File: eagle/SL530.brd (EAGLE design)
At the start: 100 x 100 mm, 42 parts, among them IC4 74LVC1G17DBV, IC5 74LVC1G17DBV, U1 LM1117, X1 MC68000

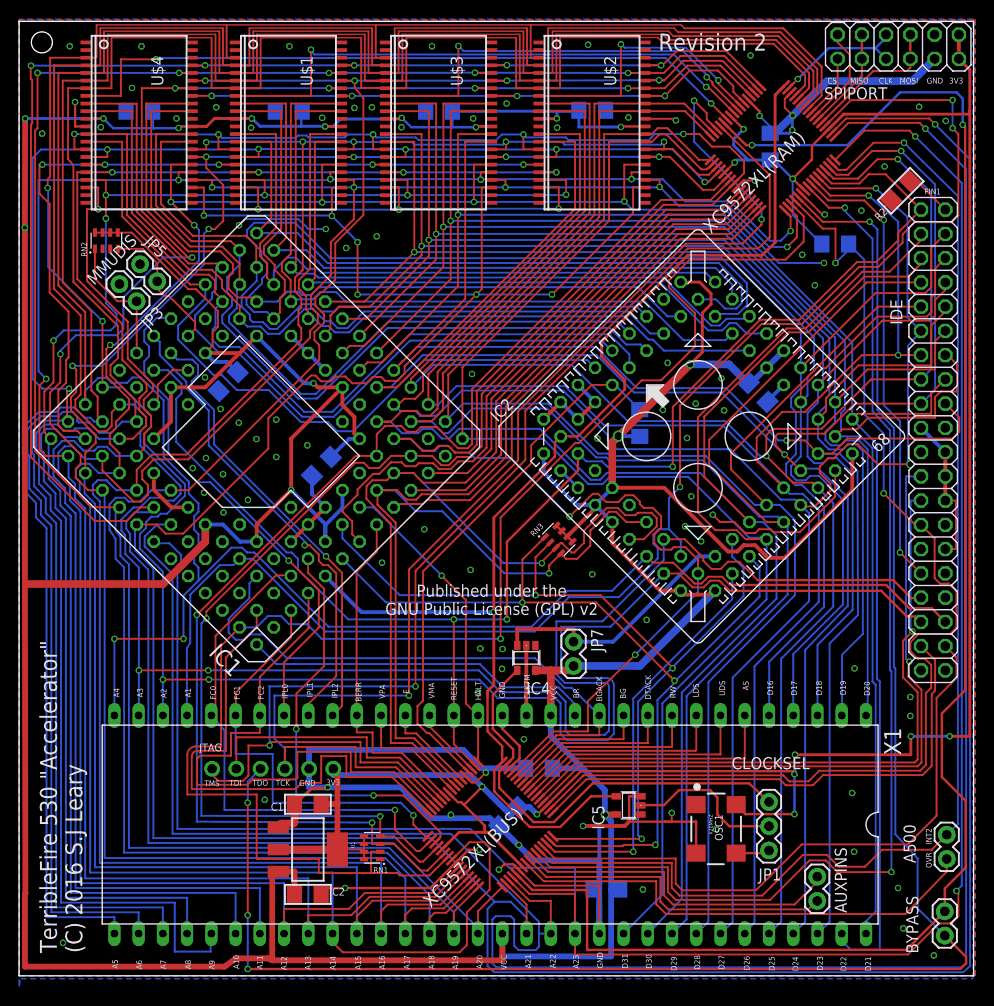
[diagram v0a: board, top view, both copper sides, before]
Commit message: Updated silkscreen
Added the CPLD orientation marks
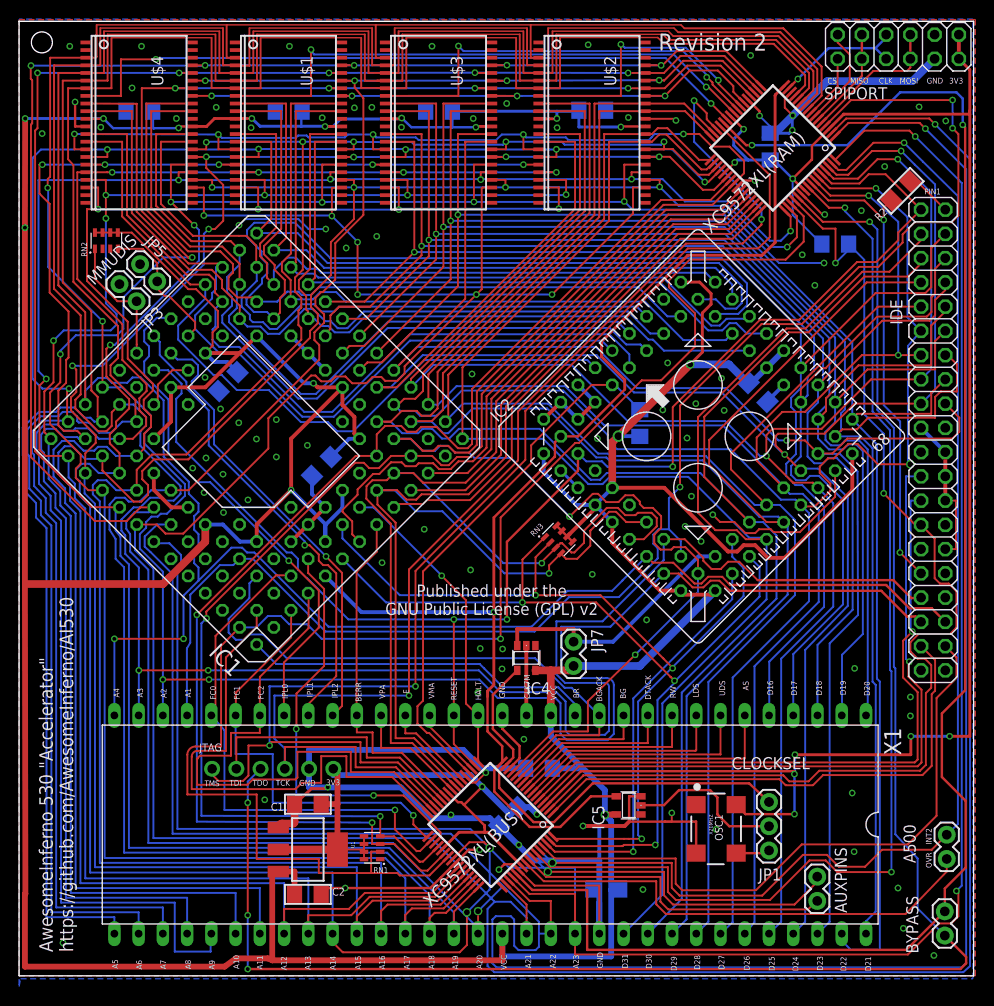
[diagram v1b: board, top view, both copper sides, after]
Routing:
- net INT2: vias 1 -> 2
- net AUX0: vias 0 -> 1
- net A20: vias 5 -> 6
- net A14: vias 7 -> 9
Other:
- board text added: "AwesomeInferno 530 "Accelerator" https://github.com/AwesomeInferno/AI530"
- board text removed: "TerribleFire 530 "Accelerator" (C) 2016 S.J Leary"
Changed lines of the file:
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@@
 <?xml version="1.0" encoding="utf-8"?>
 <!DOCTYPE eagle SYSTEM "eagle.dtd">
-<eagle version="7.7.0">
+<eagle version="7.6.0">
 <drawing>
 <settings>
@@
 <layer number="17" name="Pads" color="2" fill="1" visible="yes" active="yes"/>
 <layer number="18" name="Vias" color="2" fill="1" visible="yes" active="yes"/>
-<layer number="19" name="Unrouted" color="6" fill="1" visible="yes" active="yes"/>
+<layer number="19" name="Unrouted" color="6" fill="1" visible="no" active="yes"/>
 <layer number="20" name="Dimension" color="15" fill="1" visible="yes" active="yes"/>
 <layer number="21" name="tPlace" color="7" fill="1" visible="yes" active="yes"/>
-<layer number="22" name="bPlace" color="7" fill="1" visible="yes" active="yes"/>
-<layer number="23" name="tOrigins" color="15" fill="1" visible="yes" active="yes"/>
-<layer number="24" name="bOrigins" color="15" fill="1" visible="yes" active="yes"/>
+<layer number="22" name="bPlace" color="7" fill="1" visible="no" active="yes"/>
+<layer number="23" name="tOrigins" color="15" fill="1" visible="no" active="yes"/>
+<layer number="24" name="bOrigins" color="15" fill="1" visible="no" active="yes"/>
 <layer number="25" name="tNames" color="7" fill="1" visible="yes" active="yes"/>
 <layer number="26" name="bNames" color="7" fill="1" visible="yes" active="yes"/>
-<layer number="27" name="tValues" color="7" fill="1" visible="yes" active="yes"/>
-<layer number="28" name="bValues" color="7" fill="1" visible="yes" active="yes"/>
+<layer number="27" name="tValues" color="7" fill="1" visible="no" active="yes"/>
+<layer number="28" name="bValues" color="7" fill="1" visible="no" active="yes"/>
 <layer number="29" name="tStop" color="7" fill="3" visible="no" active="yes"/>
 <layer number="30" name="bStop" color="7" fill="6" visible="no" active="yes"/>
@@
 <layer number="49" name="Reference" color="7" fill="1" visible="no" active="yes"/>
 <layer number="50" name="dxf" color="7" fill="1" visible="no" active="no"/>
-<layer number="51" name="tDocu" color="7" fill="1" visible="yes" active="yes"/>
-<layer number="52" name="bDocu" color="7" fill="1" visible="yes" active="yes"/>
+<layer number="51" name="tDocu" color="7" fill="1" visible="no" active="yes"/>
+<layer number="52" name="bDocu" color="7" fill="1" visible="no" active="yes"/>
 <layer number="53" name="tGND_GNDA" color="7" fill="9" visible="no" active="no"/>
 <layer number="54" name="bGND_GNDA" color="1" fill="9" visible="no" active="no"/>
@@
 <text x="21.0058" y="20.4724" size="0.6096" layer="25" rot="R180">TMS</text>
 <text x="28.3718" y="20.5232" size="0.6096" layer="25" rot="R180">TCK</text>
-<text x="6.6294" y="2.3876" size="1.778" layer="25" rot="R90">TerribleFire 530 "Accelerator"
-(C) 2016 S.J Leary</text>
+<text x="5.6642" y="2.4892" size="1.4224" layer="25" rot="R90">AwesomeInferno 530 "Accelerator"
+https://github.com/AwesomeInferno/AI530</text>
 <text x="66.9798" y="96.9264" size="1.778" layer="25">Revision 2</text>
 <text x="73.406" y="75.2094" size="0.8128" layer="125" ratio="18" rot="R180">C1</text>
@@
 <text x="98.9076" y="94.0816" size="0.6096" layer="25" rot="R180">3V3</text>
 <text x="96.5454" y="82.4738" size="0.6096" layer="25" rot="R180">PIN1</text>
+<wire x1="72.4662" y1="86.7664" x2="78.9686" y2="93.2688" width="0.254" layer="21"/>
+<wire x1="78.9686" y1="93.2688" x2="85.471" y2="86.7664" width="0.254" layer="21"/>
+<wire x1="85.471" y1="86.7664" x2="85.471" y2="86.6902" width="0.127" layer="21"/>
+<wire x1="85.471" y1="86.6902" x2="78.9686" y2="80.1878" width="0.254" layer="21"/>
+<wire x1="78.9686" y1="80.1878" x2="72.4154" y2="86.741" width="0.254" layer="21"/>
+<circle x="84.455" y="86.741" radius="0.297296875" width="0.127" layer="21"/>
+<circle x="54.864" y="15.8496" radius="0.297296875" width="0.127" layer="21"/>
+<wire x1="42.8498" y1="15.9004" x2="42.9006" y2="15.9004" width="0.127" layer="21"/>
+<wire x1="42.9006" y1="15.9004" x2="49.3522" y2="22.3012" width="0.254" layer="21"/>
+<wire x1="49.3522" y1="22.3012" x2="55.9308" y2="15.7226" width="0.254" layer="21"/>
+<wire x1="55.9308" y1="15.7226" x2="55.88" y2="15.7226" width="0.127" layer="21"/>
+<wire x1="55.88" y1="15.7226" x2="49.4792" y2="9.3218" width="0.254" layer="21"/>
+<wire x1="49.4792" y1="9.3218" x2="49.4284" y2="9.3218" width="0.127" layer="21"/>
+<wire x1="49.4284" y1="9.3218" x2="42.9006" y2="15.8496" width="0.254" layer="21"/>
 </plain>
 <attributes>
@@
 <wire x1="68.8848" y1="96.8756" x2="74.0865" y2="96.8756" width="0.2032" layer="1"/>
 <wire x1="74.0865" y1="96.8756" x2="77.7057625" y2="93.2563375" width="0.2032" layer="1"/>
-<wire x1="50.615034375" y1="9.308859375" x2="48.0822" y2="6.776025" width="0.2032" layer="1"/>
+<wire x1="50.615034375" y1="9.308859375" x2="48.0822" y2="6.776025" width="0.2032" layer="16"/>
 <wire x1="1.2446" y1="54.3306" x2="1.2446" y2="89.1794" width="0.2032" layer="1"/>
 <wire x1="1.2446" y1="89.1794" x2="1.3716" y2="89.3064" width="0.2032" layer="1"/>
@@
 <wire x1="1.2192" y1="95.3262" x2="1.2446" y2="95.3516" width="0.2032" layer="1"/>
 <wire x1="1.2446" y1="54.3306" x2="7.9248" y2="47.6504" width="0.2032" layer="1"/>
+<via x="48.0822" y="6.776025" extent="1-16" drill="0.6" shape="square"/>
 </signal>
 <signal name="A19">
@@
 <wire x1="47.169846875" y1="13.9954" x2="48.7172" y2="13.9954" width="0.2032" layer="1"/>
 <wire x1="48.7172" y1="13.9954" x2="49.3014" y2="13.4112" width="0.2032" layer="1"/>
-<wire x1="49.3014" y1="13.4112" x2="49.3014" y2="9.0424" width="0.2032" layer="1"/>
-<wire x1="49.3014" y1="9.0424" x2="46.9138" y2="6.6548" width="0.2032" layer="1"/>
+<wire x1="49.3014" y1="13.4112" x2="49.3014" y2="9.0424" width="0.2032" layer="16"/>
+<wire x1="49.3014" y1="9.0424" x2="46.9138" y2="6.6548" width="0.2032" layer="16"/>
 <wire x1="46.9138" y1="6.6548" x2="46.9138" y2="3.2258" width="0.2032" layer="1"/>
 <wire x1="46.9138" y1="3.2258" x2="46.1518" y2="2.4638" width="0.2032" layer="1"/>
@@
 <wire x1="32.9184" y1="3.4544" x2="32.9184" y2="4.3434" width="0.2032" layer="1"/>
 <wire x1="32.9184" y1="4.3434" x2="32.8422" y2="4.4196" width="0.2032" layer="1"/>
+<via x="49.3014" y="13.4112" extent="1-16" drill="0.6" shape="square"/>
+<via x="46.9138" y="6.6548" extent="1-16" drill="0.6" shape="square"/>
 </signal>
 <signal name="A13">
@@
 <wire x1="68.3768" y1="11.8364" x2="68.3768" y2="9.2202" width="0.2032" layer="1"/>
 <contactref element="XC9572XL(BUS)" pad="60"/>
-<wire x1="55.86566875" y1="11.8364" x2="54.504121875" y2="13.197946875" width="0.2032" layer="1"/>
+<wire x1="55.86566875" y1="11.8364" x2="54.504121875" y2="13.197946875" width="0.2032" layer="16"/>
 <wire x1="97.1804" y1="14.7828" x2="98.3488" y2="15.9004" width="0.2032" layer="16"/>
 <wire x1="98.3488" y1="15.9004" x2="98.3488" y2="81.6864" width="0.2032" layer="16"/>
@@
 <wire x1="85.8774" y1="11.43" x2="88.6206" y2="11.43" width="0.2032" layer="1"/>
 <wire x1="88.6206" y1="11.43" x2="90.3986" y2="13.208" width="0.2032" layer="1"/>
+<via x="55.86566875" y="11.8364" extent="1-16" drill="0.6" shape="square"/>
 </signal>
 <signal name="IDECS0">
@@
 <contactref element="XC9572XL(BUS)" pad="58"/>
 <contactref element="AUXPINS" pad="1"/>
-<wire x1="53.797015625" y1="12.490840625" x2="55.39125625" y2="10.8966" width="0.2032" layer="1"/>
+<wire x1="53.797015625" y1="12.490840625" x2="55.39125625" y2="10.8966" width="0.2032" layer="16"/>
 <wire x1="55.39125625" y1="10.8966" x2="67.564" y2="10.8966" width="0.2032" layer="1"/>
 <wire x1="67.564" y1="10.8966" x2="67.564" y2="8.4328" width="0.2032" layer="1"/>
@@
 <wire x1="81.2292" y1="7.4676" x2="83.6168" y2="9.8552" width="0.2032" layer="1"/>
 <wire x1="83.6168" y1="9.8552" x2="83.6168" y2="10.3886" width="0.2032" layer="1"/>
+<via x="55.39125625" y="10.8966" extent="1-16" drill="0.6" shape="square"/>
 </signal>
 <signal name="AUX1">

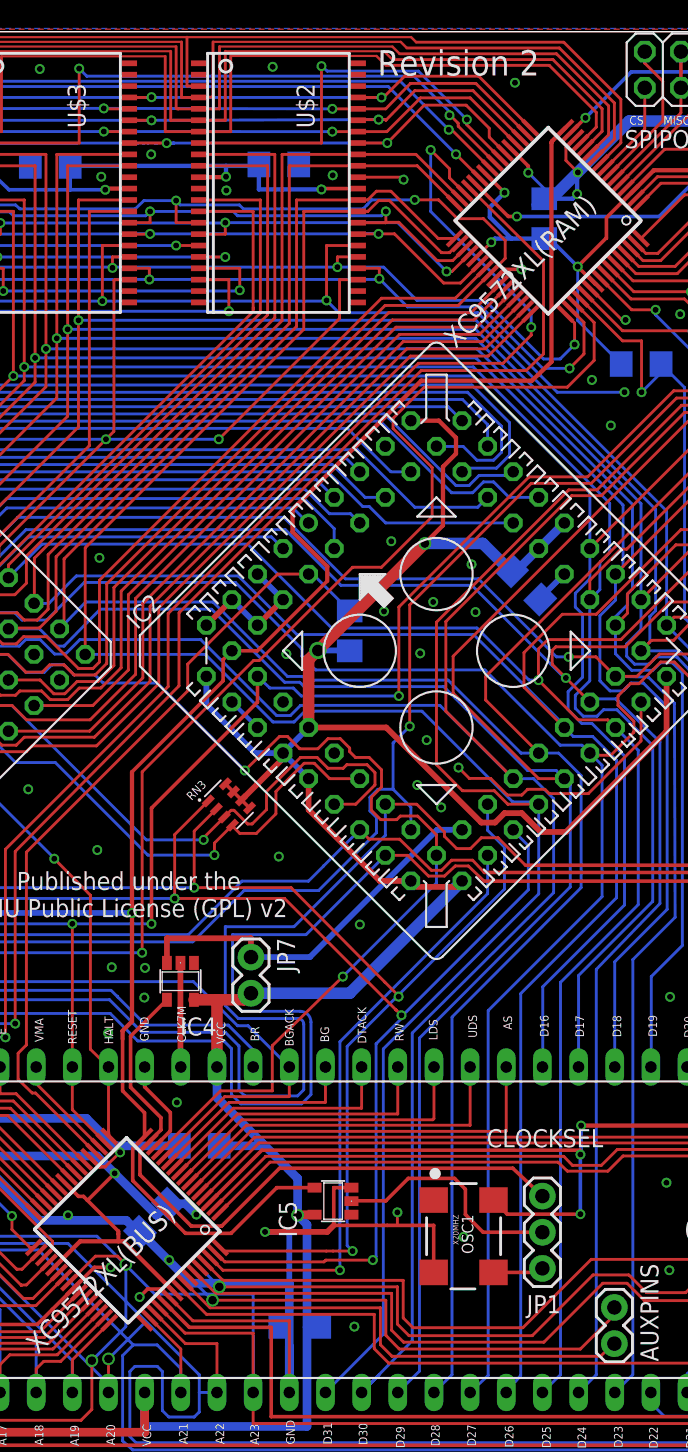
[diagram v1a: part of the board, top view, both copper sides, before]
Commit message: Misc Fixes
Fixed layer issue on BRD file (Note - right-click bad!)
Generated Gerbers
Added A500 Slot Pinout Ref.
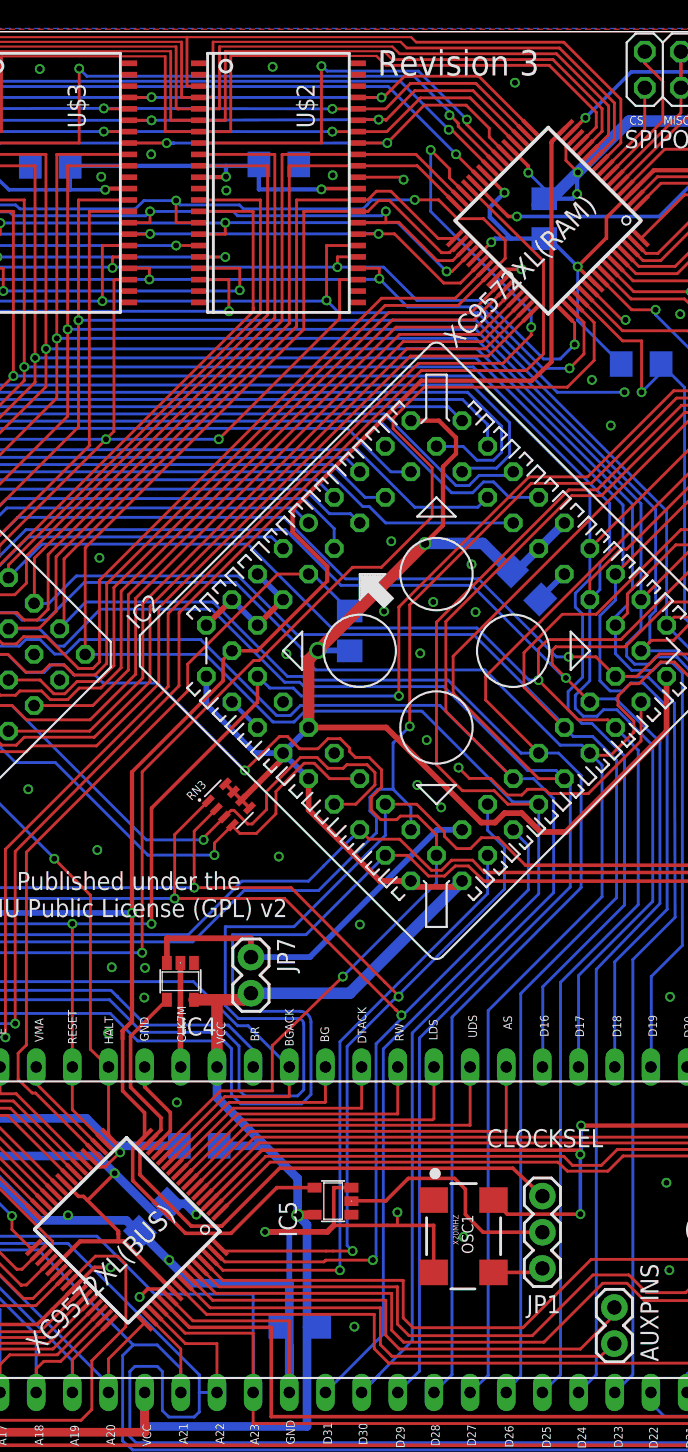
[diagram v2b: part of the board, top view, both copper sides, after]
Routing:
- net INT2: vias 2 -> 1
- net AUX0: vias 1 -> 0
- net A20: vias 6 -> 5
- net A14: vias 9 -> 7
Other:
- board text added: "Revision 3"
- board text removed: "Revision 2"
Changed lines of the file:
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@@
 <layer number="20" name="Dimension" color="15" fill="1" visible="yes" active="yes"/>
 <layer number="21" name="tPlace" color="7" fill="1" visible="yes" active="yes"/>
-<layer number="22" name="bPlace" color="7" fill="1" visible="no" active="yes"/>
+<layer number="22" name="bPlace" color="7" fill="1" visible="yes" active="yes"/>
 <layer number="23" name="tOrigins" color="15" fill="1" visible="no" active="yes"/>
 <layer number="24" name="bOrigins" color="15" fill="1" visible="no" active="yes"/>
@@
 <text x="5.6642" y="2.4892" size="1.4224" layer="25" rot="R90">AwesomeInferno 530 "Accelerator"
 https://github.com/AwesomeInferno/AI530</text>
-<text x="66.9798" y="96.9264" size="1.778" layer="25">Revision 2</text>
+<text x="66.9798" y="96.9264" size="1.778" layer="25">Revision 3</text>
 <text x="73.406" y="75.2094" size="0.8128" layer="125" ratio="18" rot="R180">C1</text>
 <text x="87.7824" y="68.7578" size="0.8128" layer="125" ratio="18">C2</text>
@@
 </class>
 </classes>
-<designrules name="dirt_cheap_dirty_boards.v1 *">
+<designrules name="dirt_cheap_dirty_boards.v1">
 <description language="en">&lt;b&gt;Dirty Cheap Dirty Board Design Rules&lt;/b&gt;
 &lt;br&gt;
@@
 <param name="mtCopper" value="0.035mm 0.0175mm 0.035mm 0.035mm 0.035mm 0.035mm 0.035mm 0.035mm 0.035mm 0.035mm 0.035mm 0.035mm 0.035mm 0.035mm 0.0175mm 0.035mm"/>
 <param name="mtIsolate" value="1.5mm 1.1mm 0.2mm 0.15mm 0.2mm 0.15mm 0.2mm 0.15mm 0.2mm 0.15mm 0.2mm 0.15mm 0.2mm 0.15mm 0.2mm"/>
-<param name="mdWireWire" value="6mil"/>
-<param name="mdWirePad" value="6mil"/>
-<param name="mdWireVia" value="6mil"/>
-<param name="mdPadPad" value="6mil"/>
-<param name="mdPadVia" value="6mil"/>
-<param name="mdViaVia" value="6mil"/>
+<param name="mdWireWire" value="5mil"/>
+<param name="mdWirePad" value="5mil"/>
+<param name="mdWireVia" value="5mil"/>
+<param name="mdPadPad" value="5mil"/>
+<param name="mdPadVia" value="5mil"/>
+<param name="mdViaVia" value="5mil"/>
 <param name="mdSmdPad" value="0mil"/>
 <param name="mdSmdVia" value="0mil"/>
@@
 <param name="mdDrill" value="10mil"/>
 <param name="mdSmdStop" value="0mil"/>
-<param name="msWidth" value="6mil"/>
+<param name="msWidth" value="5mil"/>
 <param name="msDrill" value="12mil"/>
 <param name="msMicroVia" value="12mil"/>
@@
 <wire x1="68.8848" y1="96.8756" x2="74.0865" y2="96.8756" width="0.2032" layer="1"/>
 <wire x1="74.0865" y1="96.8756" x2="77.7057625" y2="93.2563375" width="0.2032" layer="1"/>
-<wire x1="50.615034375" y1="9.308859375" x2="48.0822" y2="6.776025" width="0.2032" layer="16"/>
+<wire x1="50.615034375" y1="9.308859375" x2="48.0822" y2="6.776025" width="0.2032" layer="1"/>
 <wire x1="1.2446" y1="54.3306" x2="1.2446" y2="89.1794" width="0.2032" layer="1"/>
 <wire x1="1.2446" y1="89.1794" x2="1.3716" y2="89.3064" width="0.2032" layer="1"/>
@@
 <wire x1="1.2192" y1="95.3262" x2="1.2446" y2="95.3516" width="0.2032" layer="1"/>
 <wire x1="1.2446" y1="54.3306" x2="7.9248" y2="47.6504" width="0.2032" layer="1"/>
-<via x="48.0822" y="6.776025" extent="1-16" drill="0.6" shape="square"/>
 </signal>
 <signal name="A19">
@@
 <wire x1="47.169846875" y1="13.9954" x2="48.7172" y2="13.9954" width="0.2032" layer="1"/>
 <wire x1="48.7172" y1="13.9954" x2="49.3014" y2="13.4112" width="0.2032" layer="1"/>
-<wire x1="49.3014" y1="13.4112" x2="49.3014" y2="9.0424" width="0.2032" layer="16"/>
-<wire x1="49.3014" y1="9.0424" x2="46.9138" y2="6.6548" width="0.2032" layer="16"/>
+<wire x1="49.3014" y1="13.4112" x2="49.3014" y2="9.0424" width="0.2032" layer="1"/>
+<wire x1="49.3014" y1="9.0424" x2="46.9138" y2="6.6548" width="0.2032" layer="1"/>
 <wire x1="46.9138" y1="6.6548" x2="46.9138" y2="3.2258" width="0.2032" layer="1"/>
 <wire x1="46.9138" y1="3.2258" x2="46.1518" y2="2.4638" width="0.2032" layer="1"/>
@@
 <wire x1="32.9184" y1="3.4544" x2="32.9184" y2="4.3434" width="0.2032" layer="1"/>
 <wire x1="32.9184" y1="4.3434" x2="32.8422" y2="4.4196" width="0.2032" layer="1"/>
-<via x="49.3014" y="13.4112" extent="1-16" drill="0.6" shape="square"/>
-<via x="46.9138" y="6.6548" extent="1-16" drill="0.6" shape="square"/>
 </signal>
 <signal name="A13">
@@
 <wire x1="68.3768" y1="11.8364" x2="68.3768" y2="9.2202" width="0.2032" layer="1"/>
 <contactref element="XC9572XL(BUS)" pad="60"/>
-<wire x1="55.86566875" y1="11.8364" x2="54.504121875" y2="13.197946875" width="0.2032" layer="16"/>
+<wire x1="55.86566875" y1="11.8364" x2="54.504121875" y2="13.197946875" width="0.2032" layer="1"/>
 <wire x1="97.1804" y1="14.7828" x2="98.3488" y2="15.9004" width="0.2032" layer="16"/>
 <wire x1="98.3488" y1="15.9004" x2="98.3488" y2="81.6864" width="0.2032" layer="16"/>
@@
 <wire x1="85.8774" y1="11.43" x2="88.6206" y2="11.43" width="0.2032" layer="1"/>
 <wire x1="88.6206" y1="11.43" x2="90.3986" y2="13.208" width="0.2032" layer="1"/>
-<via x="55.86566875" y="11.8364" extent="1-16" drill="0.6" shape="square"/>
 </signal>
 <signal name="IDECS0">
@@
 <contactref element="XC9572XL(BUS)" pad="58"/>
 <contactref element="AUXPINS" pad="1"/>
-<wire x1="53.797015625" y1="12.490840625" x2="55.39125625" y2="10.8966" width="0.2032" layer="16"/>
+<wire x1="53.797015625" y1="12.490840625" x2="55.39125625" y2="10.8966" width="0.2032" layer="1"/>
 <wire x1="55.39125625" y1="10.8966" x2="67.564" y2="10.8966" width="0.2032" layer="1"/>
 <wire x1="67.564" y1="10.8966" x2="67.564" y2="8.4328" width="0.2032" layer="1"/>
@@
 <wire x1="81.2292" y1="7.4676" x2="83.6168" y2="9.8552" width="0.2032" layer="1"/>
 <wire x1="83.6168" y1="9.8552" x2="83.6168" y2="10.3886" width="0.2032" layer="1"/>
-<via x="55.39125625" y="10.8966" extent="1-16" drill="0.6" shape="square"/>
 </signal>
 <signal name="AUX1">
